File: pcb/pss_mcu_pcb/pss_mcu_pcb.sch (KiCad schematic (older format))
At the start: 50 parts, among them J1 STM32_Prog, J2 UART_Prog, J3 Conn_01x18, J4 Conn_01x18, SW1 Boot, SW2 EN, SW3 SW_Push, U1 LM3940IMP-3.3_NOPB, U2 LM358, U3 STM32F030K6Tx, U4 ESP32-WROOM-32U

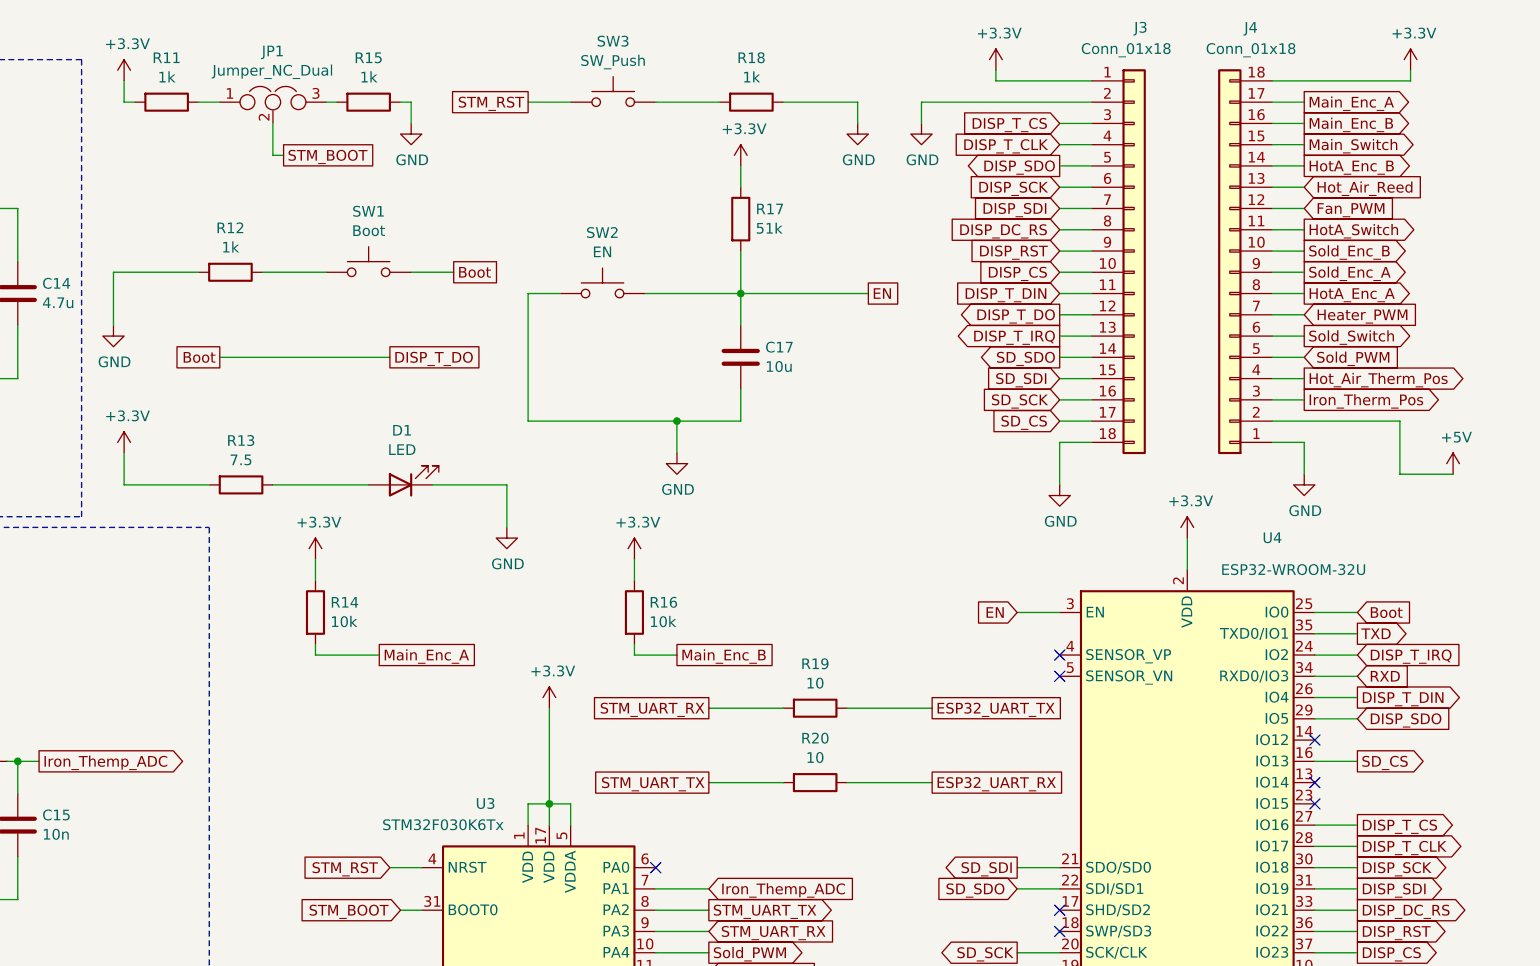
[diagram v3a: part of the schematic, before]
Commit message: Add new routes
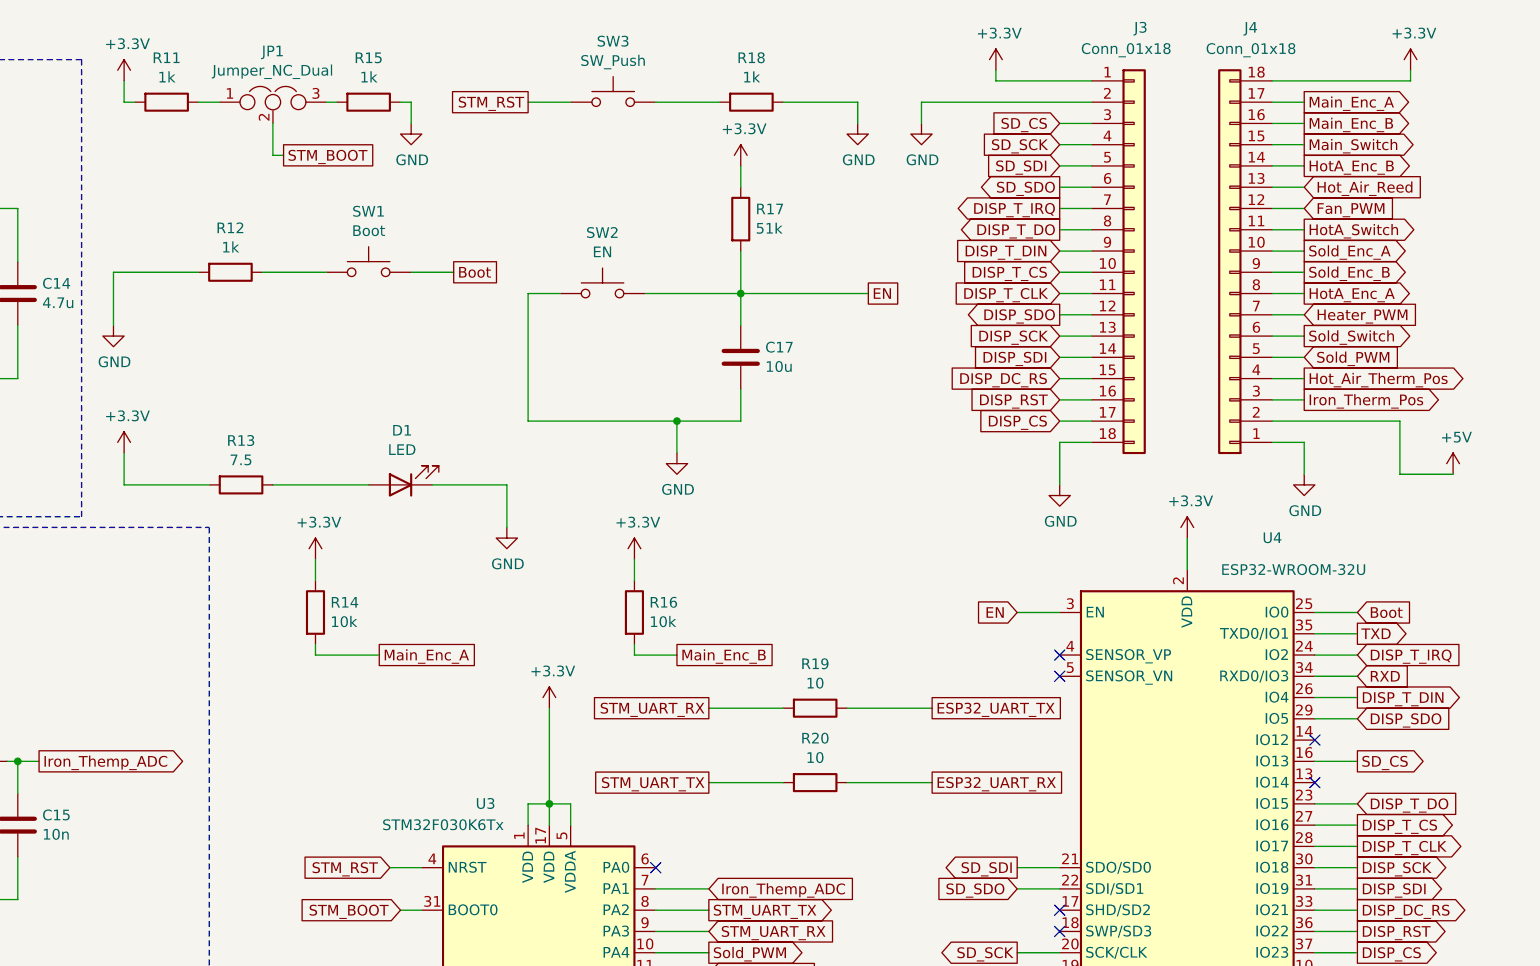
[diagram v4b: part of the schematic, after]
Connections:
- net Boot: no longer J3.12 (Pin_12)
- net DISP_CS: now also J3.17 (Pin_17); no longer J3.10 (Pin_10)
- net DISP_DC_RS: now also J3.15 (Pin_15); no longer J3.8 (Pin_8)
- net DISP_RST: now also J3.16 (Pin_16); no longer J3.9 (Pin_9)
- net DISP_SCK: now also J3.13 (Pin_13); no longer J3.6 (Pin_6)
- net DISP_SDI: now also J3.14 (Pin_14); no longer J3.7 (Pin_7)
- net DISP_SDO: now also J3.12 (Pin_12); no longer J3.5 (Pin_5)
- net DISP_T_CLK: now also J3.11 (Pin_11); no longer J3.4 (Pin_4)
- net DISP_T_CS: now also J3.10 (Pin_10); no longer J3.3 (Pin_3)
- net DISP_T_DIN: now also J3.9 (Pin_9); no longer J3.11 (Pin_11)
- net DISP_T_IRQ: now also J3.7 (Pin_7); no longer J3.13 (Pin_13)
- net SD_CS: now also J3.3 (Pin_3); no longer J3.17 (Pin_17)
- net SD_SCK: now also J3.4 (Pin_4); no longer J3.16 (Pin_16)
- net SD_SDI: now also J3.5 (Pin_5); no longer J3.15 (Pin_15)
- net SD_SDO: now also J3.6 (Pin_6); no longer J3.14 (Pin_14)
- net Sold_Enc_A: now also J4.10 (Pin_10); no longer J4.9 (Pin_9)
- net Sold_Enc_B: now also J4.9 (Pin_9); no longer J4.10 (Pin_10)
- net DISP_T_DO: now reaches U4.23 (IO15)
- net DISP_T_DO: now also J3.8 (Pin_8)
- no-connect marks 19 -> 18
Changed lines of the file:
@@
 Wire Wire Line
 	6200 1700 6400 1700
-Text GLabel 5300 2100 0    50   UnSpc ~ 0
-Boot
-Text GLabel 6100 2100 2    50   UnSpc ~ 0
-DISP_T_DO
-Wire Wire Line
-	5300 2100 6100 2100
 Text GLabel 7450 3500 2    50   UnSpc ~ 0
 Main_Enc_B
@@
 	10650 5100 10450 5100
 NoConn ~ 10450 5000
-NoConn ~ 10450 4200
 NoConn ~ 10450 4100
 NoConn ~ 9250 3600
@@
 Text GLabel 10400 900  2    50   Output ~ 0
 Main_Enc_A
-Text GLabel 9250 1500 0    50   Input ~ 0
+Text GLabel 9250 2200 0    50   Input ~ 0
 DISP_DC_RS
+Text GLabel 9250 2400 0    50   Input ~ 0
+DISP_CS
+Text GLabel 9250 2100 0    50   Input ~ 0
+DISP_SDI
+Text GLabel 9250 2000 0    50   Input ~ 0
+DISP_SCK
+Text GLabel 9250 2300 0    50   Input ~ 0
+DISP_RST
+Text GLabel 9250 1800 0    50   Input ~ 0
+DISP_T_CLK
 Text GLabel 9250 1700 0    50   Input ~ 0
-DISP_CS
-Text GLabel 9250 1400 0    50   Input ~ 0
-DISP_SDI
-Text GLabel 9250 1300 0    50   Input ~ 0
-DISP_SCK
+DISP_T_CS
 Text GLabel 9250 1600 0    50   Input ~ 0
-DISP_RST
-Text GLabel 9250 1100 0    50   Input ~ 0
-DISP_T_CLK
+DISP_T_DIN
+Text GLabel 9250 1500 0    50   Output ~ 0
+DISP_T_DO
+Text GLabel 9250 1400 0    50   Output ~ 0
+DISP_T_IRQ
+Text GLabel 9250 1900 0    50   Output ~ 0
+DISP_SDO
 Text GLabel 9250 1000 0    50   Input ~ 0
-DISP_T_CS
-Text GLabel 9250 1800 0    50   Input ~ 0
-DISP_T_DIN
-Text GLabel 9250 1900 0    50   Output ~ 0
-DISP_T_DO
-Text GLabel 9250 2000 0    50   Output ~ 0
-DISP_T_IRQ
-Text GLabel 9250 1200 0    50   Output ~ 0
-DISP_SDO
-Text GLabel 9250 2400 0    50   Input ~ 0
 SD_CS
 Wire Wire Line
 	10250 2000 10400 2000
-Text GLabel 9250 2200 0    50   Input ~ 0
+Text GLabel 9250 1200 0    50   Input ~ 0
 SD_SDI
 $Comp
@@
 Wire Wire Line
 	10250 1200 10400 1200
-Text GLabel 9250 2300 0    50   Input ~ 0
+Text GLabel 9250 1100 0    50   Input ~ 0
 SD_SCK
-Text GLabel 9250 2100 0    50   Output ~ 0
+Text GLabel 9250 1300 0    50   Output ~ 0
 SD_SDO
 $Comp
@@
 Wire Wire Line
 	10250 1300 10400 1300
-Text GLabel 10400 1700 2    50   Output ~ 0
-Sold_Enc_A
 Text GLabel 10400 2200 2    50   Output ~ 0
 Hot_Air_Therm_Pos
@@
 NoConn ~ 6250 6000
 NoConn ~ 7350 4500
-Text GLabel 10400 1800 2    50   Output ~ 0
-HotA_Enc_A
-Text GLabel 10400 1600 2    50   Output ~ 0
+Text GLabel 10400 1700 2    50   Output ~ 0
 Sold_Enc_B
 Text GLabel 10400 1500 2    50   Output ~ 0
@@
 	7350 4600 7600 4600
 NoConn ~ 6250 5400
+Text GLabel 10400 1800 2    50   Output ~ 0
+HotA_Enc_A
+Text GLabel 10400 1600 2    50   Output ~ 0
+Sold_Enc_A
+Text GLabel 10650 4200 2    50   Input ~ 0
+DISP_T_DO
+Wire Wire Line
+	10650 4200 10450 4200
 $EndSCHEMATC

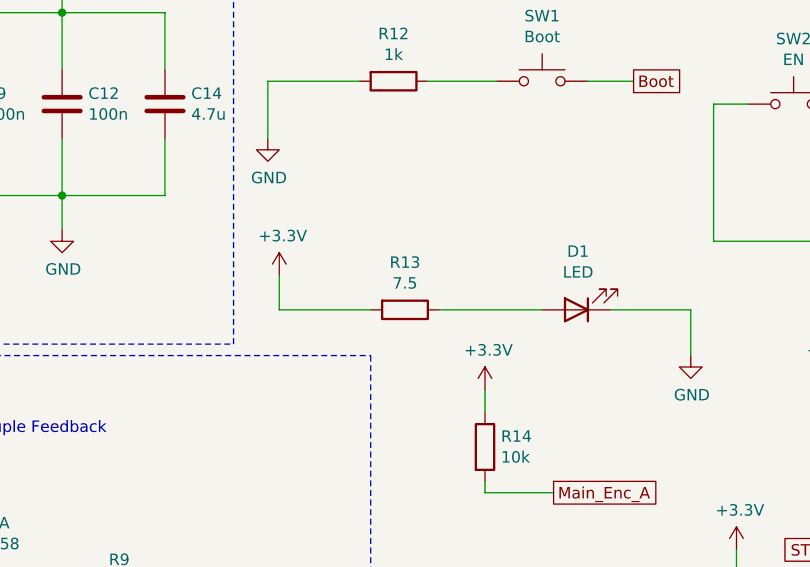
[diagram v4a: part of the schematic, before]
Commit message: Change resistor value
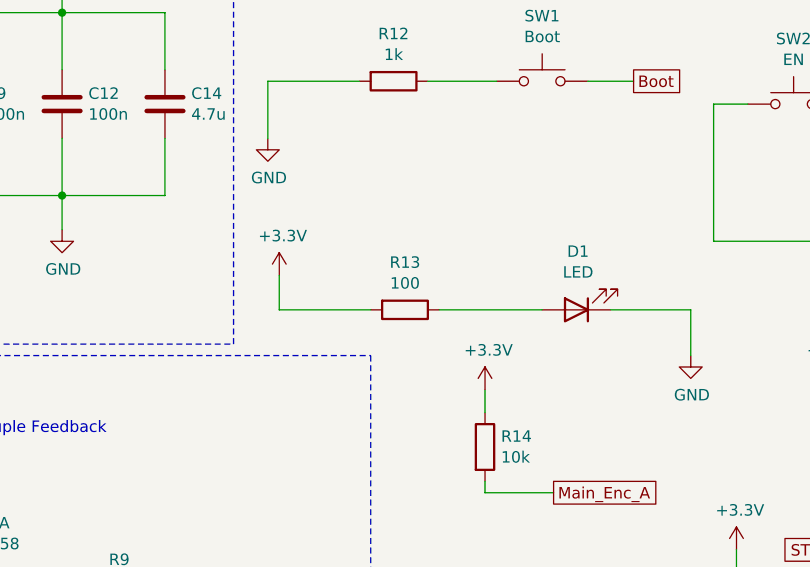
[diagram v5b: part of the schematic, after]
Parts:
- R13: value 7.5 -> 100
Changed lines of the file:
@@
 P 5400 2700
 F 0 "R13" V 5193 2700 50  0000 C CNN
-F 1 "7.5" V 5284 2700 50  0000 C CNN
+F 1 "100" V 5284 2700 50  0000 C CNN
 F 2 "Resistor_SMD:R_0603_1608Metric_Pad0.98x0.95mm_HandSolder" V 5330 2700 50  0001 C CNN
 F 3 "~" H 5400 2700 50  0001 C CNN
